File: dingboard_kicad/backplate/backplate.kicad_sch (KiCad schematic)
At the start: 2 parts, among them J1 10018784-10210TLF, J2 Bus_PCI_Express_x1

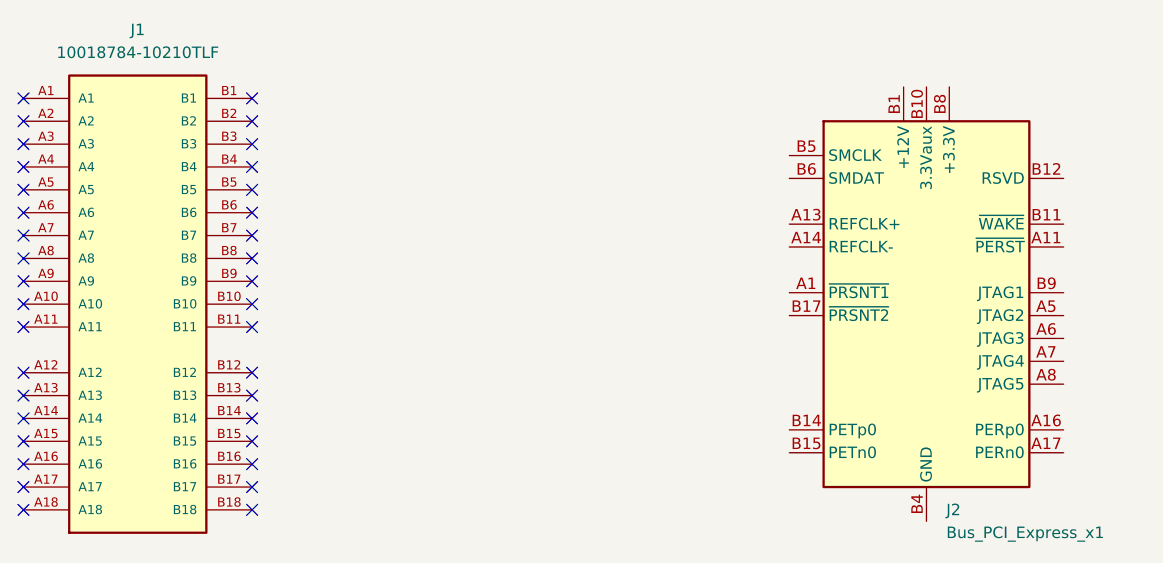
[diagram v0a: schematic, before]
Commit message: place BME680 in dingboard sensors schematic
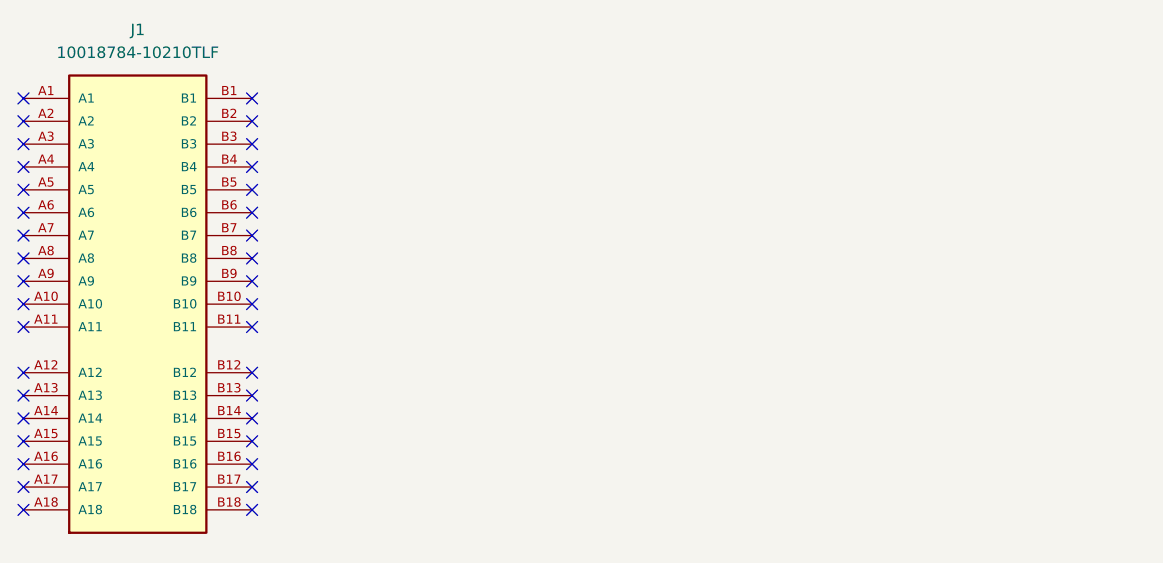
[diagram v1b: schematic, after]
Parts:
- removed J2: Bus_PCI_Express_x1, Connector_PCBEdge:BUS_PCIexpress_x1, symbol Connector:Bus_PCI_Express_x1
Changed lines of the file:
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@@
-		)
-	)
-	(symbol
-		(lib_id "Connector:Bus_PCI_Express_x1")
-		(at 215.9 90.17 0)
-		(unit 1)
-		(exclude_from_sim no)
-		(in_bom yes)
-		(on_board yes)
-		(dnp no)
-		(fields_autoplaced yes)
-		(property "Reference" "J2"
-			(at 218.0941 111.76 0)
-			(effects
-				(font
-					(size 1.27 1.27)
-				)
-				(justify left)
-			)
-		)
-		(property "Value" "Bus_PCI_Express_x1"
-			(at 218.0941 114.3 0)
-			(effects
-				(font
-					(size 1.27 1.27)
-				)
-				(justify left)
-			)
-		)
-		(property "Footprint" "Connector_PCBEdge:BUS_PCIexpress_x1"
-			(at 215.9 97.79 0)
-			(effects
-				(font
-					(size 1.27 1.27)
-				)
-				(hide yes)
-			)
-		)
-		(property "Datasheet" "http://www.ritrontek.com/uploadfile/2016/1026/20161026105231124.pdf#page=63"
-			(at 209.55 109.22 0)
-			(effects
-				(font
-					(size 1.27 1.27)
-				)
-				(hide yes)
-			)
-		)
-		(property "Description" "PCI Express bus connector x1"
-			(at 215.9 90.17 0)
-			(effects
-				(font
-					(size 1.27 1.27)
-				)
-				(hide yes)
-			)
-		)
-		(pin "A12"
-		)
-		(pin "B6"
-		)
-		(pin "B7"
-		)
-		(pin "B4"
-		)
-		(pin "B5"
-		)
-		(pin "B17"
-		)
-		(pin "B18"
-		)
-		(pin "B15"
-		)
-		(pin "B16"
-		)
-		(pin "B2"
-		)
-		(pin "B3"
-		)
-		(pin "A13"
-		)
-		(pin "B8"
-		)
-		(pin "B9"
-		)
-		(pin "A8"
-		)
-		(pin "A9"
-		)
-		(pin "A6"
-		)
-		(pin "A7"
-		)
-		(pin "B13"
-		)
-		(pin "B14"
-		)
-		(pin "B11"
-		)
-		(pin "B12"
-		)
-		(pin "A15"
-		)
-		(pin "A14"
-		)
-		(pin "A11"
-		)
-		(pin "B1"
-		)
-		(pin "B10"
-		)
-		(pin "A3"
-		)
-		(pin "A10"
-		)
-		(pin "A2"
-		)
-		(pin "A1"
-		)
-		(pin "A16"
-		)
-		(pin "A5"
-		)
-		(pin "A18"
-		)
-		(pin "A4"
-		)
-		(pin "A17"
-		)
-		(instances
-			(project ""
-				(path "/3ac1a34a-3a2d-4f8e-be23-a5fa61208278"
-					(reference "J2")
-					(unit 1)
-				)
-			)
 		)
 	)
